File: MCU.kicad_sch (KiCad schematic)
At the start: 32 parts, among them J1 Conn_ARM_SWD_TagConnect_TC2030, U1 STM32WB55CGUx, U2 W25Q128JVP, U3 MLPF-WB55-01E3, X1 32MHz, X2 32kHz768

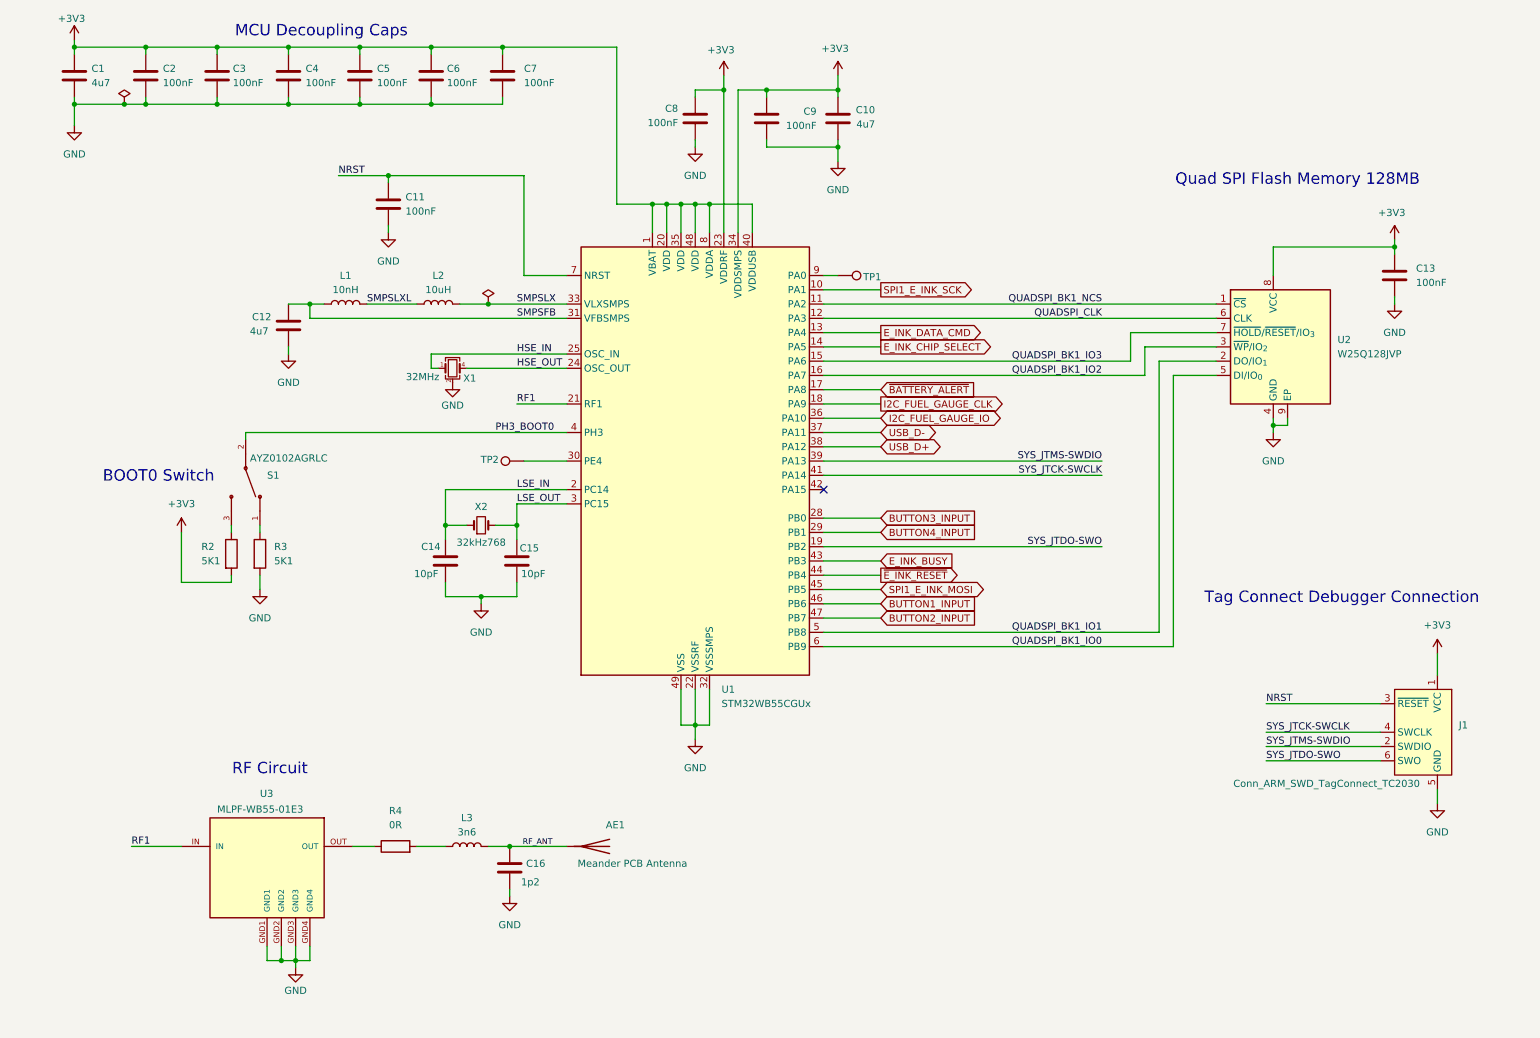
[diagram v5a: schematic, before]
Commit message: Choose footprints for all parts
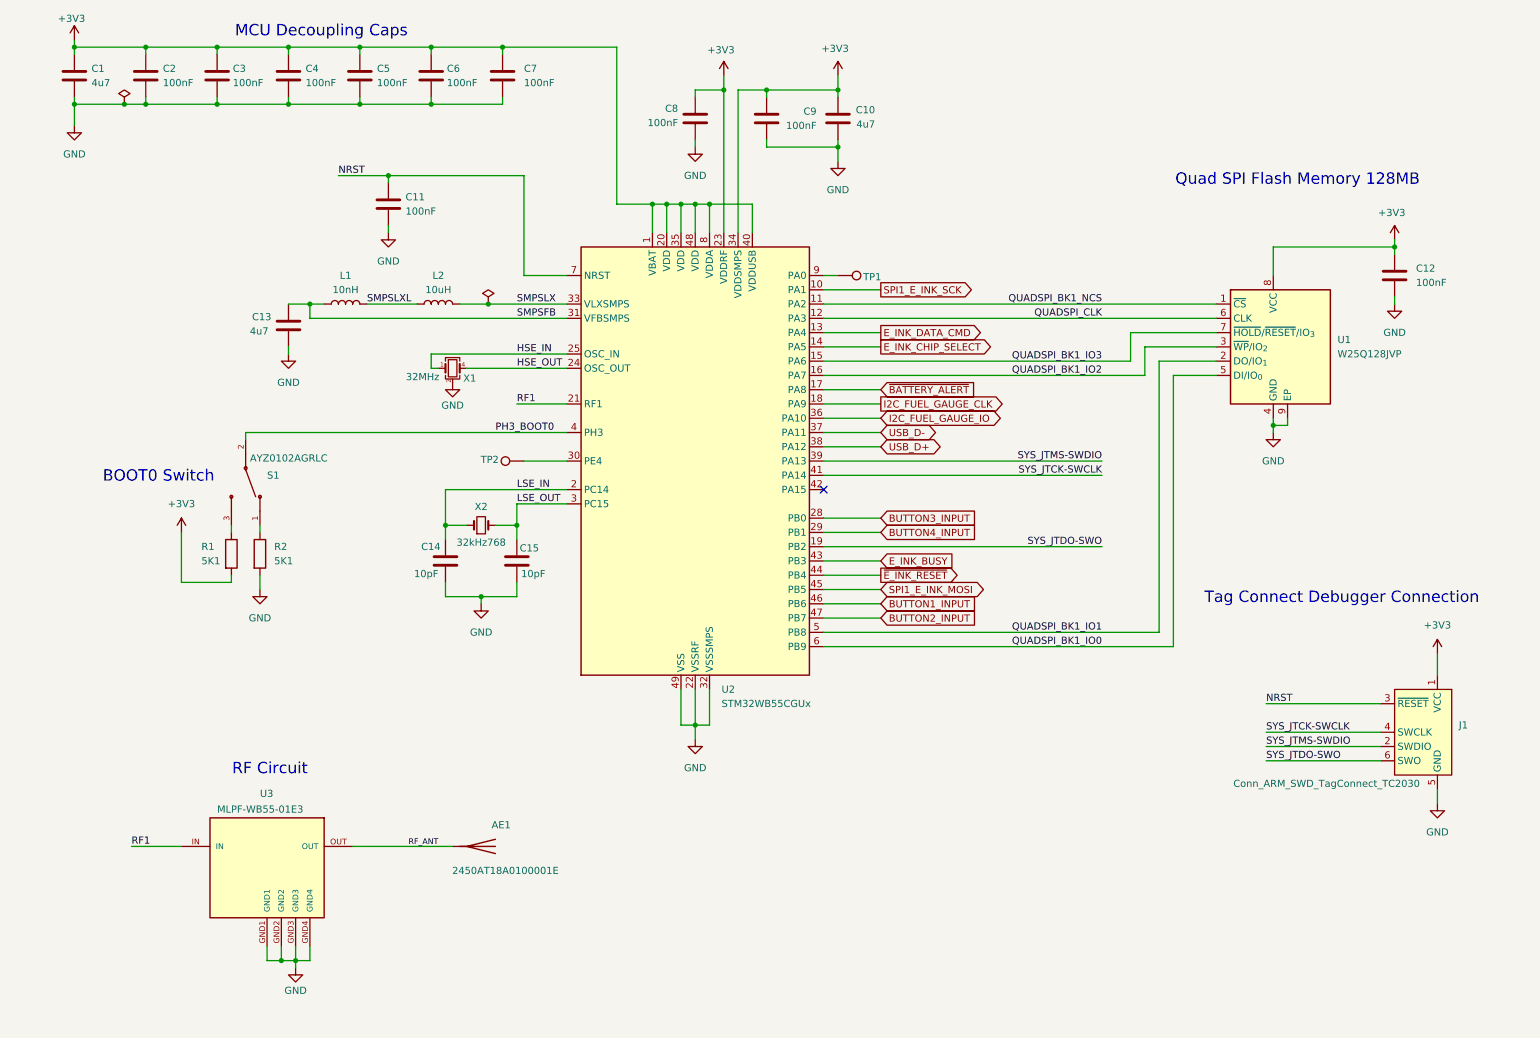
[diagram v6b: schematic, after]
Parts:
- removed C16: 1p2, symbol Device:C
- removed L3: 3n6, symbol Device:L
- removed R4: 0R, Resistor_SMD:R_0402_1005Metric, symbol Device:R
- AE1: value Meander PCB Antenna -> 2450AT18A0100001E; footprint (none) -> LibraryFootprints:XCVR_2450AT18A0100001E
- C1, C10: footprint (none) -> Capacitor_SMD:C_0603_1608Metric
- C13: renamed from C12; footprint (none) -> Capacitor_SMD:C_0603_1608Metric
- C14, C15: footprint (none) -> Capacitor_SMD:C_0402_1005Metric
- L1: footprint (none) -> Inductor_SMD:L_0402_1005Metric
- L2: footprint (none) -> Inductor_SMD:L_0805_2012Metric
- R1: renamed from R2; footprint (none) -> Resistor_SMD:R_0402_1005Metric
- R2: renamed from R3; footprint (none) -> Resistor_SMD:R_0402_1005Metric
- X1: footprint (none) -> Crystal:Crystal_SMD_2016-4Pin_2.0x1.6mm
- X2: footprint (none) -> Crystal:Crystal_SMD_2012-2Pin_2.0x1.2mm; MPN (none) -> NX2012_32K768
- renumbered C13 to C12, U2 to U1, U1 to U2
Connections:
- net RF_ANT: now also U3.OUT
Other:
- moved on the sheet: AE1

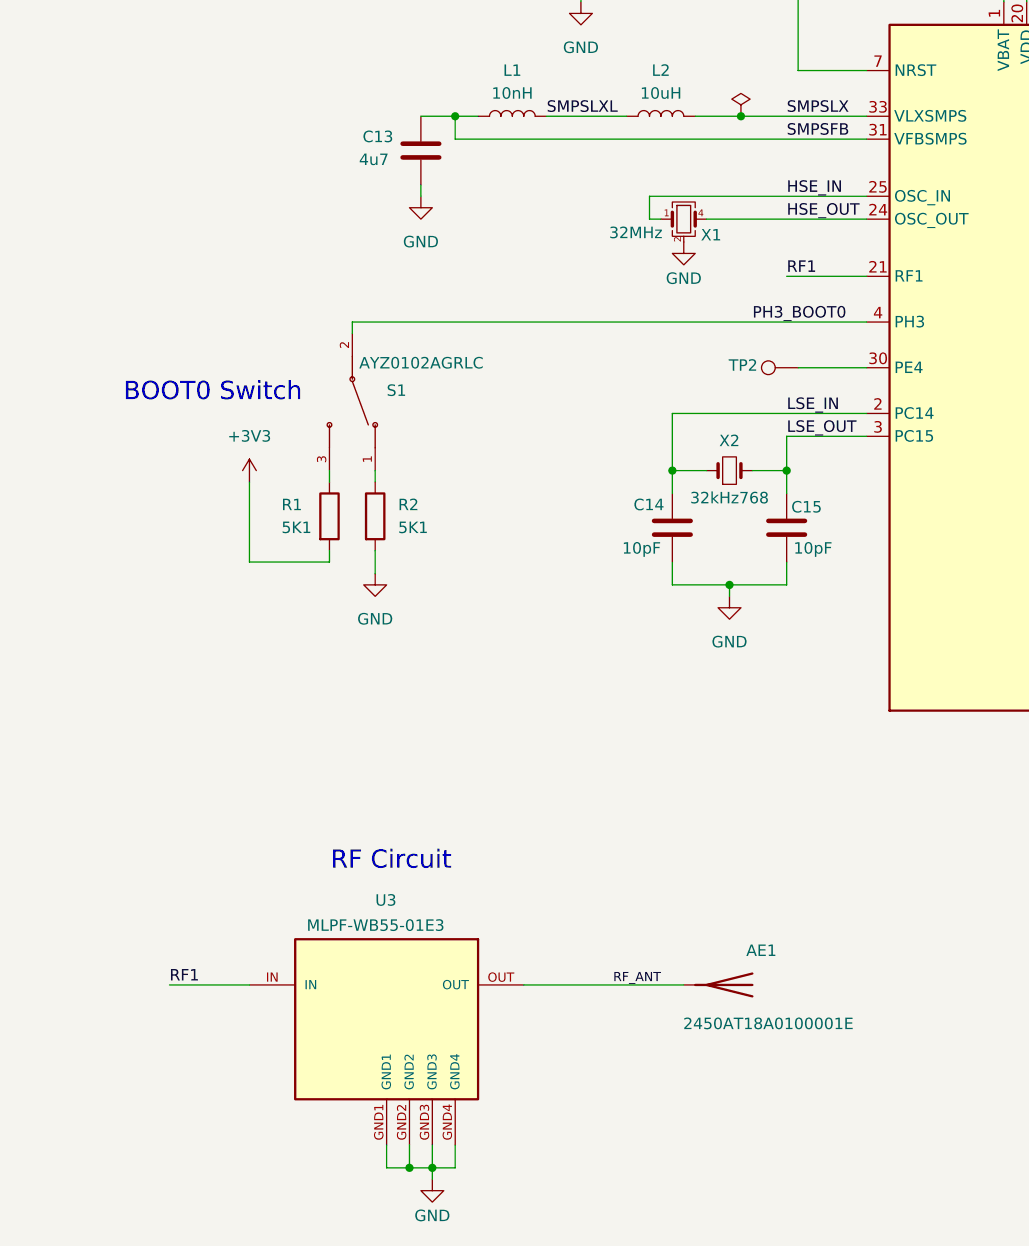
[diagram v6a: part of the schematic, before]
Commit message: Added layout rules and constraints
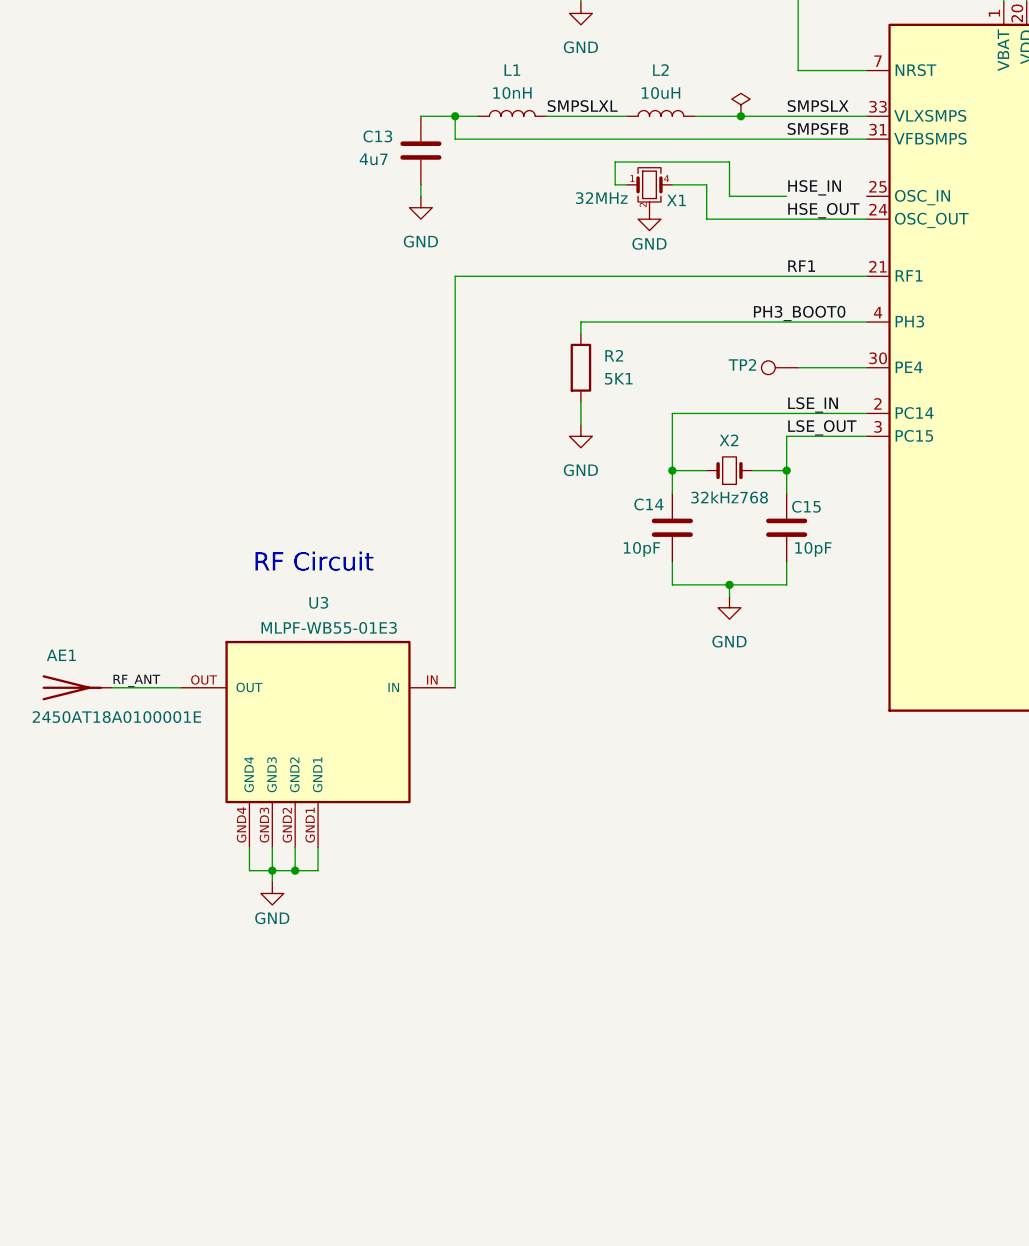
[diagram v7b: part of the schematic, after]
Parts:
- removed R1: 5K1, Resistor_SMD:R_0402_1005Metric, symbol Device:R
- removed S1: AYZ0102AGRLC, LibraryFootprints:SW_AYZ0102AGRLC, symbol AYZ0102AGRLC:AYZ0102AGRLC
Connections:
- net HSE_IN: no longer U2.25 (OSC_IN)
- net PH3_BOOT0: now also R2.1
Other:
- note removed: "BOOT0 Switch"
- moved on the sheet: AE1, R2, U3, X1
